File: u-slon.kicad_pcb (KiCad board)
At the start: 2 copper layers, 135 x 91 mm, 71 parts, among them CON1 AVR-ISP-10, IC1 ATMEGA8A-M, J1 USB_B, P4 ST-020, P5 ST-020, Q1 IRFL4310, Q2 IRFL4310, Q3 IRFL4310, U1 AD823, X1 12MHz

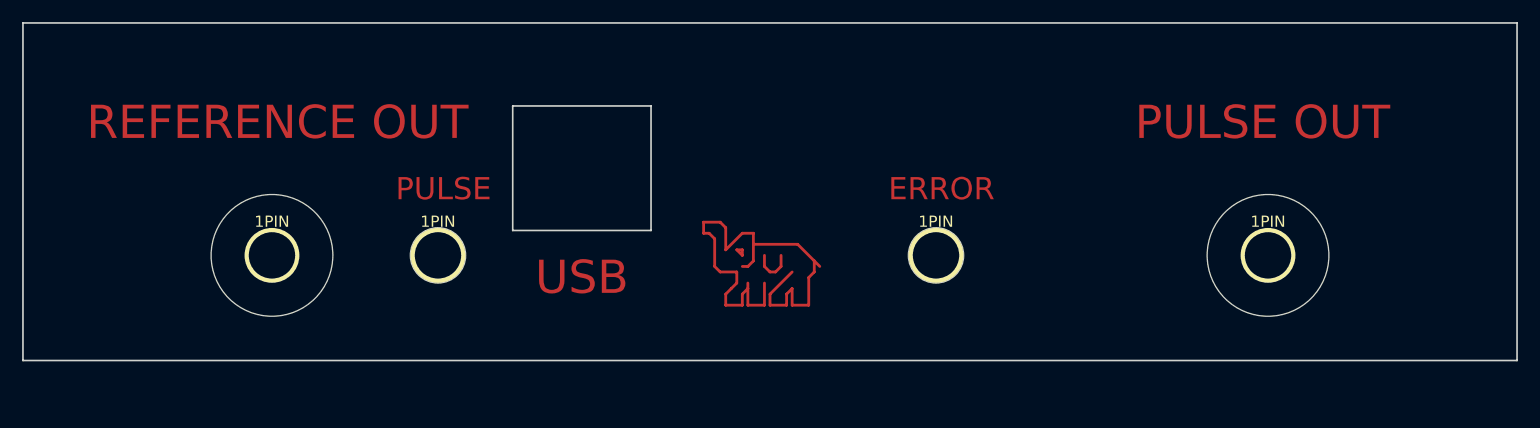
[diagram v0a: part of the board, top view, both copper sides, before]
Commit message: Face was extracted and removed from this file.
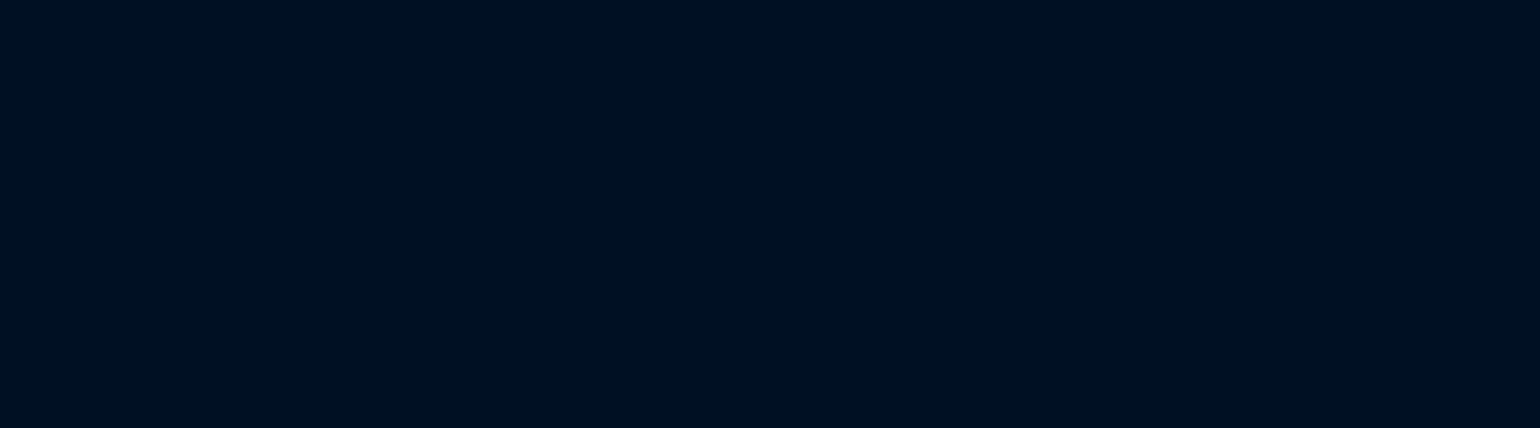
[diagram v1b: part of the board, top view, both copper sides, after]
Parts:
- removed 1PIN (x4): P***, 1pin
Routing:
- net (no net): track 113.5 -> 56.8 mm
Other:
- board size 135 x 91 mm -> 110 x 40 mm
- board text removed: "ERROR"
- board text removed: "FACE FOR GAINTA G706 CASE"
- board text removed: "PULSE"
- board text removed: "PULSE OUT"
- board text removed: "REFERENCE OUT"
- board text removed: "USB"
